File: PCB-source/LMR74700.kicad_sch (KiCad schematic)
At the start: 4 parts, among them Q1 AO3400A, U4 LM74700

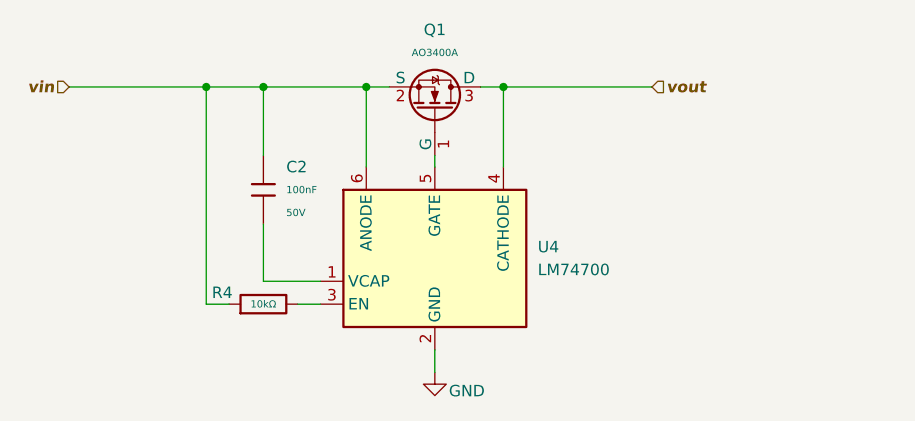
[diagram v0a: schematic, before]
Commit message: Finish component and diffpair placement
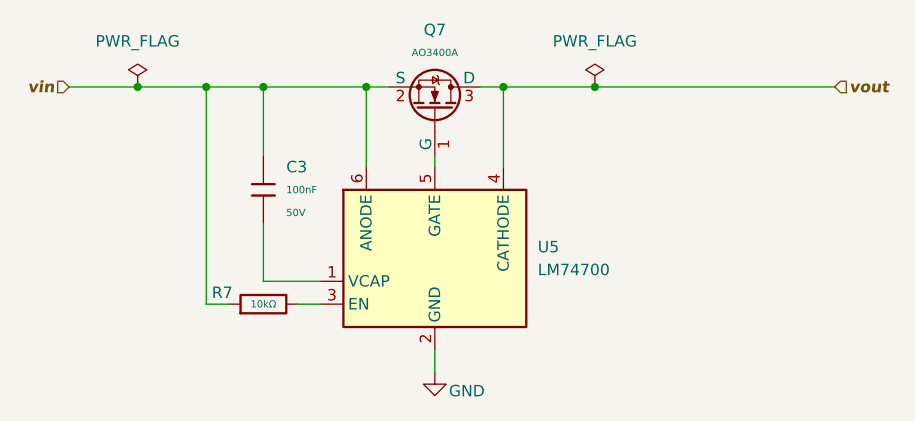
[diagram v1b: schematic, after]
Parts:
- renumbered C2 to C3, Q1 to Q7, R4 to R7, U4 to U5
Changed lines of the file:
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@@
+	)
+	(junction
+		(at 116.84 80.01)
+		(diameter 0)
+		(color 0 0 0 0)
+	)
+	(junction
+		(at 167.64 80.01)
+		(diameter 0)
+		(color 0 0 0 0)
 	)
 	(junction
@@
 	(wire
 		(pts
+			(xy 167.64 80.01) (xy 194.31 80.01)
+		)
+		(stroke
+			(width 0)
+			(type default)
+		)
+	)
+	(wire
+		(pts
 			(xy 127 104.14) (xy 124.46 104.14)
 		)
@@
 	(wire
 		(pts
-			(xy 157.48 80.01) (xy 173.99 80.01)
+			(xy 157.48 80.01) (xy 167.64 80.01)
 		)
 		(stroke
@@
 	(wire
 		(pts
-			(xy 109.22 80.01) (xy 124.46 80.01)
+			(xy 116.84 80.01) (xy 124.46 80.01)
+		)
+		(stroke
+			(width 0)
+			(type default)
+		)
+	)
+	(wire
+		(pts
+			(xy 109.22 80.01) (xy 116.84 80.01)
 		)
 		(stroke
@@
 	(hierarchical_label "vout"
 		(shape input)
-		(at 173.99 80.01 0)
+		(at 194.31 80.01 0)
 		(effects
 			(font
@@
 			)
 			(justify left)
+		)
+	)
+	(symbol
+		(lib_id "power:PWR_FLAG")
+		(at 167.64 80.01 0)
+		(unit 1)
+		(exclude_from_sim no)
+		(in_bom yes)
+		(on_board yes)
+		(dnp no)
+		(fields_autoplaced yes)
+		(property "Reference" "#FLG03"
+			(at 167.64 78.105 0)
+			(effects
+				(font
+					(size 1.27 1.27)
+				)
+				(hide yes)
+			)
+		)
+		(property "Value" "PWR_FLAG"
+			(at 167.64 74.93 0)
+			(effects
+				(font
+					(size 1.27 1.27)
+				)
+			)
+		)
+		(property "Footprint" ""
+			(at 167.64 80.01 0)
+			(effects
+				(font
+					(size 1.27 1.27)
+				)
+				(hide yes)
+			)
+		)
+		(property "Datasheet" "~"
+			(at 167.64 80.01 0)
+			(effects
+				(font
+					(size 1.27 1.27)
+				)
+				(hide yes)
+			)
+		)
+		(property "Description" "Special symbol for telling ERC where power comes from"
+			(at 167.64 80.01 0)
+			(effects
+				(font
+					(size 1.27 1.27)
+				)
+				(hide yes)
+			)
+		)
+		(pin "1"
+		)
+		(instances
+			(project "MMS2"
+				(path "/6596548a-44e0-46d8-8624-fd71cf4a3e17/c3406df1-7cb0-4484-a477-0c72b46ba076/f6350a3a-247d-4669-ac4a-852f0d340cf0"
+					(reference "#FLG03")
+					(unit 1)
+				)
+			)
+		)
+	)
+	(symbol
+		(lib_id "power:PWR_FLAG")
+		(at 116.84 80.01 0)
+		(unit 1)
+		(exclude_from_sim no)
+		(in_bom yes)
+		(on_board yes)
+		(dnp no)
+		(fields_autoplaced yes)
+		(property "Reference" "#FLG02"
+			(at 116.84 78.105 0)
+			(effects
+				(font
+					(size 1.27 1.27)
+				)
+				(hide yes)
+			)
+		)
+		(property "Value" "PWR_FLAG"
+			(at 116.84 74.93 0)
+			(effects
+				(font
+					(size 1.27 1.27)
+				)
+			)
+		)
+		(property "Footprint" ""
+			(at 116.84 80.01 0)
+			(effects
+				(font
+					(size 1.27 1.27)
+				)
+				(hide yes)
+			)
+		)
+		(property "Datasheet" "~"
+			(at 116.84 80.01 0)
+			(effects
+				(font
+					(size 1.27 1.27)
+				)
+				(hide yes)
+			)
+		)
+		(property "Description" "Special symbol for telling ERC where power comes from"
+			(at 116.84 80.01 0)
+			(effects
+				(font
+					(size 1.27 1.27)
+				)
+				(hide yes)
+			)
+		)
+		(pin "1"
+		)
+		(instances
+			(project "MMS2"
+				(path "/6596548a-44e0-46d8-8624-fd71cf4a3e17/c3406df1-7cb0-4484-a477-0c72b46ba076/f6350a3a-247d-4669-ac4a-852f0d340cf0"
+					(reference "#FLG02")
+					(unit 1)
+				)
+			)
 		)
 	)
@@
 		(dnp no)
 		(fields_autoplaced yes)
-		(property "Reference" "Q1"
+		(property "Reference" "Q7"
 			(at 149.86 73.66 90)
 			(effects
@@
 		(instances
 			(project "MMS2"
-				(path "/6596548a-44e0-46d8-8624-fd71cf4a3e17/c3406df1-7cb0-4484-a477-0c72b46ba076/cdc43f49-31e3-4312-b1a3-409f3aaffb4d"
-					(reference "Q4")
-					(unit 1)
-				)
-				(path "/6596548a-44e0-46d8-8624-fd71cf4a3e17/c3406df1-7cb0-4484-a477-0c72b46ba076/f60c8d37-96ca-4d01-b39d-56f0787a1018"
-					(reference "Q1")
-					(unit 1)
-				)
 				(path "/6596548a-44e0-46d8-8624-fd71cf4a3e17/c3406df1-7cb0-4484-a477-0c72b46ba076/f6350a3a-247d-4669-ac4a-852f0d340cf0"
 					(reference "Q7")
@@
 		(on_board yes)
 		(dnp no)
-		(property "Reference" "R4"
+		(property "Reference" "R7"
 			(at 126.238 102.87 90)
 			(effects
@@
 		(instances
 			(project "MMS2"
-				(path "/6596548a-44e0-46d8-8624-fd71cf4a3e17/c3406df1-7cb0-4484-a477-0c72b46ba076/cdc43f49-31e3-4312-b1a3-409f3aaffb4d"
-					(reference "R6")
-					(unit 1)
-				)
-				(path "/6596548a-44e0-46d8-8624-fd71cf4a3e17/c3406df1-7cb0-4484-a477-0c72b46ba076/f60c8d37-96ca-4d01-b39d-56f0787a1018"
-					(reference "R4")
-					(unit 1)
-				)
 				(path "/6596548a-44e0-46d8-8624-fd71cf4a3e17/c3406df1-7cb0-4484-a477-0c72b46ba076/f6350a3a-247d-4669-ac4a-852f0d340cf0"
 					(reference "R7")
@@
 		(dnp no)
 		(fields_autoplaced yes)
-		(property "Reference" "C2"
+		(property "Reference" "C3"
 			(at 133.35 88.8999 0)
 			(effects
@@
 		(instances
 			(project "MMS2"
-				(path "/6596548a-44e0-46d8-8624-fd71cf4a3e17/c3406df1-7cb0-4484-a477-0c72b46ba076/cdc43f49-31e3-4312-b1a3-409f3aaffb4d"
-					(reference "C1")
-					(unit 1)
-				)
-				(path "/6596548a-44e0-46d8-8624-fd71cf4a3e17/c3406df1-7cb0-4484-a477-0c72b46ba076/f60c8d37-96ca-4d01-b39d-56f0787a1018"
-					(reference "C2")
-					(unit 1)
-				)
 				(path "/6596548a-44e0-46d8-8624-fd71cf4a3e17/c3406df1-7cb0-4484-a477-0c72b46ba076/f6350a3a-247d-4669-ac4a-852f0d340cf0"
 					(reference "C3")
@@
 		(dnp no)
 		(fields_autoplaced yes)
-		(property "Reference" "U4"
+		(property "Reference" "U5"
 			(at 161.29 97.7899 0)
 			(effects
@@
 		(instances
 			(project "MMS2"
-				(path "/6596548a-44e0-46d8-8624-fd71cf4a3e17/c3406df1-7cb0-4484-a477-0c72b46ba076/cdc43f49-31e3-4312-b1a3-409f3aaffb4d"
-					(reference "U3")
-					(unit 1)
-				)
-				(path "/6596548a-44e0-46d8-8624-fd71cf4a3e17/c3406df1-7cb0-4484-a477-0c72b46ba076/f60c8d37-96ca-4d01-b39d-56f0787a1018"
-					(reference "U4")
-					(unit 1)
-				)
 				(path "/6596548a-44e0-46d8-8624-fd71cf4a3e17/c3406df1-7cb0-4484-a477-0c72b46ba076/f6350a3a-247d-4669-ac4a-852f0d340cf0"
 					(reference "U5")
@@
 		(on_board yes)
 		(dnp no)
-		(property "Reference" "#PWR011"
+		(property "Reference" "#PWR012"
 			(at 149.86 118.11 0)
 			(effects
@@
 		(instances
 			(project "MMS2"
-				(path "/6596548a-44e0-46d8-8624-fd71cf4a3e17/c3406df1-7cb0-4484-a477-0c72b46ba076/cdc43f49-31e3-4312-b1a3-409f3aaffb4d"
-					(reference "#PWR020")
-					(unit 1)
-				)
-				(path "/6596548a-44e0-46d8-8624-fd71cf4a3e17/c3406df1-7cb0-4484-a477-0c72b46ba076/f60c8d37-96ca-4d01-b39d-56f0787a1018"
-					(reference "#PWR011")
-					(unit 1)
-				)
 				(path "/6596548a-44e0-46d8-8624-fd71cf4a3e17/c3406df1-7cb0-4484-a477-0c72b46ba076/f6350a3a-247d-4669-ac4a-852f0d340cf0"
 					(reference "#PWR012")
